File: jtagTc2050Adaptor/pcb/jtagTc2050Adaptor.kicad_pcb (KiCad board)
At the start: 2 copper layers, 49.5 x 35.6 mm, 26 parts, among them CON1 10PIN_JTAG_SWD, P1 CONN_01X02, P10 CONN_01X03, P2 CONN_01X01, P3 CONN_01X03, P4 CONN_01X03, P5 USB_OTG, P6 CONN_02X10, P7 CONN_02X03, P9 CONN_01X03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

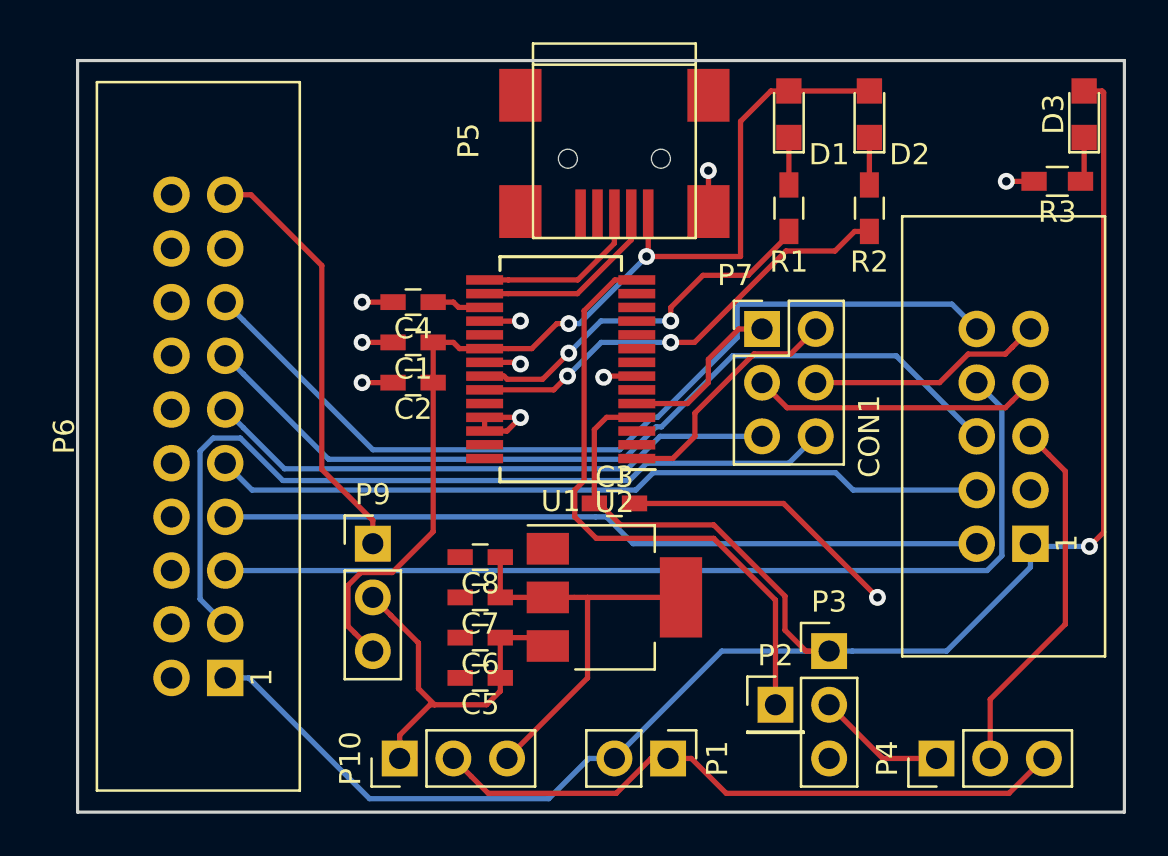
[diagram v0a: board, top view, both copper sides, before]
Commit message: finished jtagTc2050Adaptor Layout
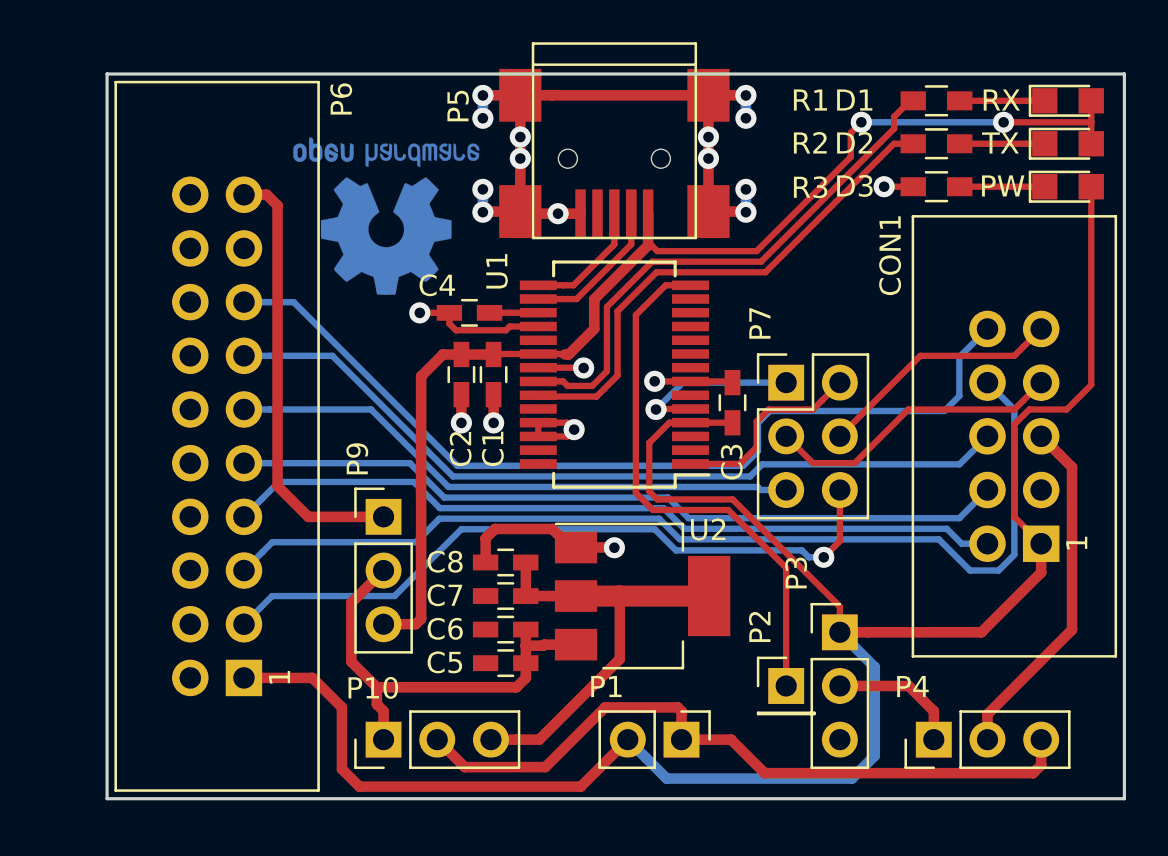
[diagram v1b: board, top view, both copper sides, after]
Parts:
- added G***: LOGO, proz_logo:Shimatta_SolderMask, B.Cu at (77.9, 76.1)
- added REF***: KiCad-Logo2_6mm_SilkScreen, Symbols:KiCad-Logo2_6mm_SilkScreen, B.Cu at (93.5, 71.6)
- added REF***: OSHW-Logo2_9.8x8mm_Copper, Symbols:OSHW-Logo2_9.8x8mm_Copper, B.Cu at (65.4, 72.1)
- moved D1 13.2 mm to (97.7, 66.7), turned to 0 degrees
- moved D2 9.50 mm to (97.7, 68.7), turned to 0 degrees
- moved R1 8.64 mm to (91.4, 66.7), turned to 180 degrees
- moved C3 7.34 mm to (81.8, 81.0), turned to 90 degrees
- moved R3 5.72 mm to (91.4, 70.7)
- moved R2 4.40 mm to (91.4, 68.7), turned to 180 degrees
- moved C1 4.10 mm to (70.5, 79.6), turned to 270 degrees
- moved D3 3.51 mm to (97.7, 70.7), turned to 0 degrees
- moved P7 2.79 mm to (84.3, 80.0)
- moved C4 2.71 mm to (69.3, 76.7)
- moved U1 2.55 mm to (76.2, 79.6)
- moved C2 2.32 mm to (69.0, 79.6), turned to 270 degrees
- moved C5 1.40 mm to (71.1, 93.3)
- moved P9 1.37 mm to (65.3, 86.4)
- moved U2 1.34 mm to (77.5, 90.1)
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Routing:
- net GND: track 30.3 -> 62.6 mm, vias 10 -> 21
- net /RXLED: track 17.8 -> 25.5 mm, vias 2 -> 0
- net /nTRST: track 39.8 -> 33.3 mm, vias 0 -> 1
- net +5V: track 49.2 -> 55.4 mm
- net /PROGMODE_FT: track 29.1 -> 25.7 mm
- net Net-(C5-Pad1): track 18.0 -> 21.2 mm
- net /TXLED: track 21.3 -> 24.5 mm, vias 2 -> 0
- net /TARGET_SUPPLY: track 30.7 -> 33.7 mm
- net /TDO: track 41.2 -> 38.3 mm
- net Net-(P5-Pad3): track 8.26 -> 5.85 mm
- net Net-(P5-Pad2): track 9.23 -> 6.92 mm
- net /TxD: track 11.7 -> 9.37 mm
- net Net-(D3-Pad1): track 2.15 -> 4.02 mm
- net Net-(D2-Pad1): track 2.25 -> 4.02 mm
- net Net-(D1-Pad1): track 2.25 -> 4.02 mm
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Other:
- board size 49.5 x 35.6 mm -> 48.1 x 34.3 mm
- board text added: "3V3"
- board text added: "5V"
- board text added: "COM"
- board text added: "FT"
- board text added: "GND"
- board text added: "JTAG"
- board text added: "PW"
- board text added: "RX"
- board text added: "SWD"
- board text added: "Supply"
- board text added: "TX"
- board text added: "Target Supply"
- board text added: "USB"
- board text added: "VCC"
- board text added: "VCC = Supply"
- board text added: "progmode"

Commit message: finished layout for avrIspMk2Clone
generated documentation and gerber files
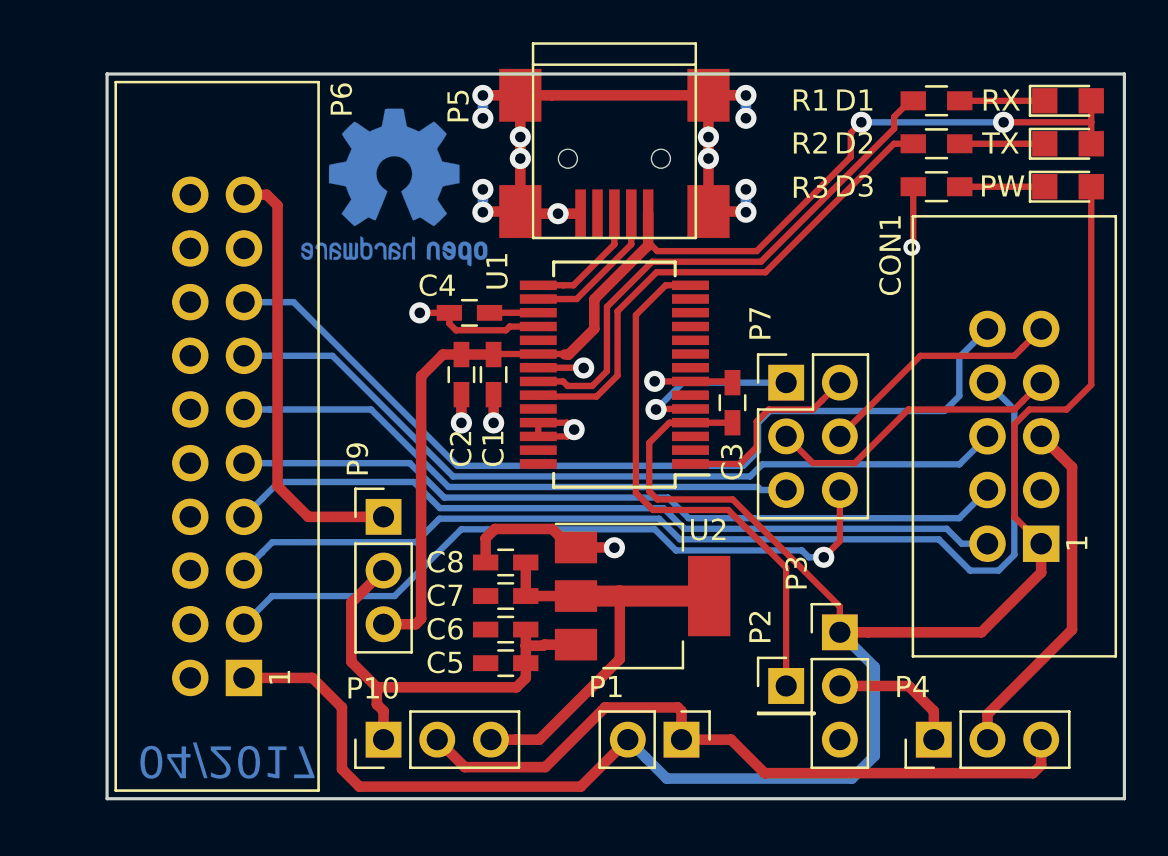
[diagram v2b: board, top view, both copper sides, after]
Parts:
- removed the REF*** at (93.5, 71.6)
- added REF**: KiCAD Logo, Symbols:Symbol_KiCAD-Logo_CopperAndSilkScreenTop, B.Cu at (93.6, 70.8)
- moved G*** 2.68 mm to (80.4, 75.3), turned to 180 degrees
- moved REF*** 1.42 mm to (65.8, 70.8), turned to 180 degrees
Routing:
- net GND: track 62.6 -> 64.1 mm
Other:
- board text added: "04/2017"
